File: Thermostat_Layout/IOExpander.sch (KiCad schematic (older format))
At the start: 9 parts, among them J4 Conn_01x04, J5 Conn_01x10, U4 TLP3545, U5 MCP23017_SO, U6 TLP3545, U7 TLP3545

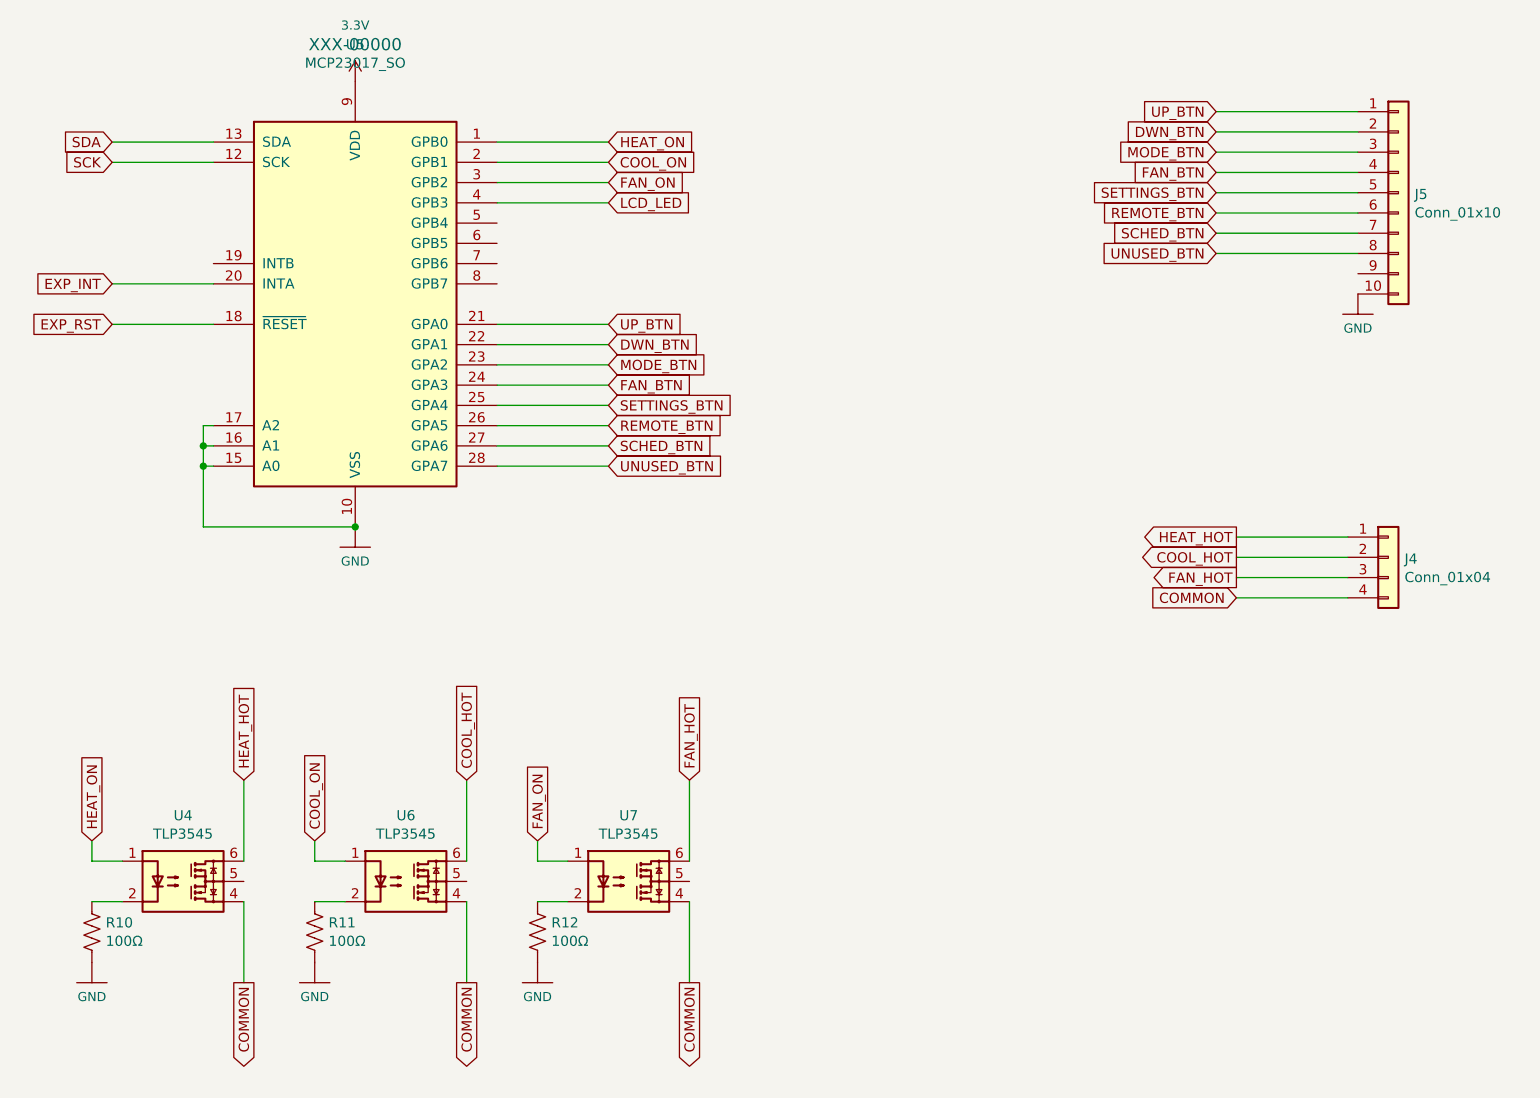
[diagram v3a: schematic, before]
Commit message: Schematic and PCB layout for thermostat
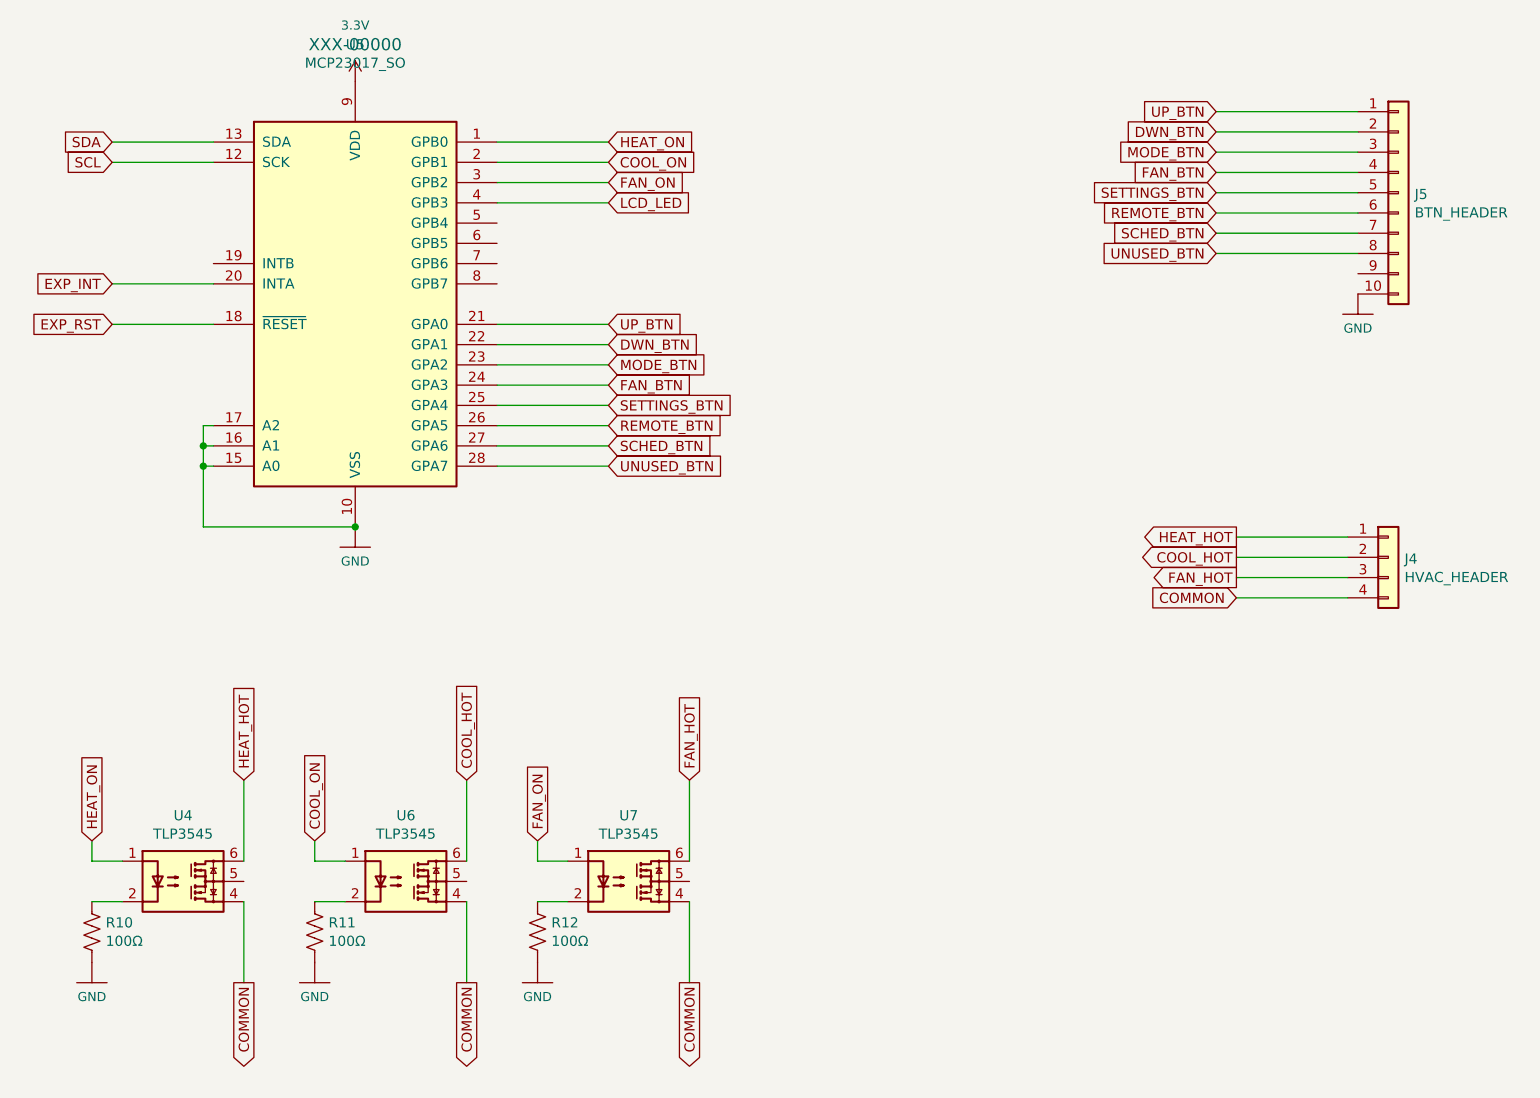
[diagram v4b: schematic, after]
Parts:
- J4: value Conn_01x04 -> HVAC_HEADER
- J5: value Conn_01x10 -> BTN_HEADER
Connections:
- net SCK renamed SCL
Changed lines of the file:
@@
 EXP_RST
 Text GLabel 2550 2100 0    50   Input ~ 0
-SCK
+SCL
 Text GLabel 2550 2000 0    50   Input ~ 0
 SDA
@@
 P 8900 2250
 F 0 "J5" H 8980 2242 50  0000 L CNN
-F 1 "Conn_01x10" H 8980 2151 50  0000 L CNN
+F 1 "BTN_HEADER" H 8980 2151 50  0000 L CNN
 F 2 "Connector_JST:JST_PH_S10B-PH-SM4-TB_1x10-1MP_P2.00mm_Horizontal" H 8900 2250 50  0001 C CNN
 F 3 "~" H 8900 2250 50  0001 C CNN
@@
 P 8850 4050
 F 0 "J4" H 8930 4042 50  0000 L CNN
-F 1 "Conn_01x04" H 8930 3951 50  0000 L CNN
+F 1 "HVAC_HEADER" H 8930 3951 50  0000 L CNN
 F 2 "TerminalBlock_TE-Connectivity:TerminalBlock_TE_282834-4_1x04_P2.54mm_Horizontal" H 8850 4050 50  0001 C CNN
 F 3 "~" H 8850 4050 50  0001 C CNN
